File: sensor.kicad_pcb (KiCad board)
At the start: 2 copper layers, 62 x 65 mm, 94 parts, among them CON1 Micro USB, CON2 PROG, CON3 Jack-DC, CON4 HTU21D, CON5 Conn_01x08, Q1 BSS214N, Q2 BSS214N, Q3 BSS214N, Q4 BSP716N, Q5 BSP716N, Q6 BSP716N, SW1 RESET, SW2 CFG, U1 LM7805, U2 TLV1117LV33DCY, U3 ESP-12F, U4 HTU21D, U5 PMS7003

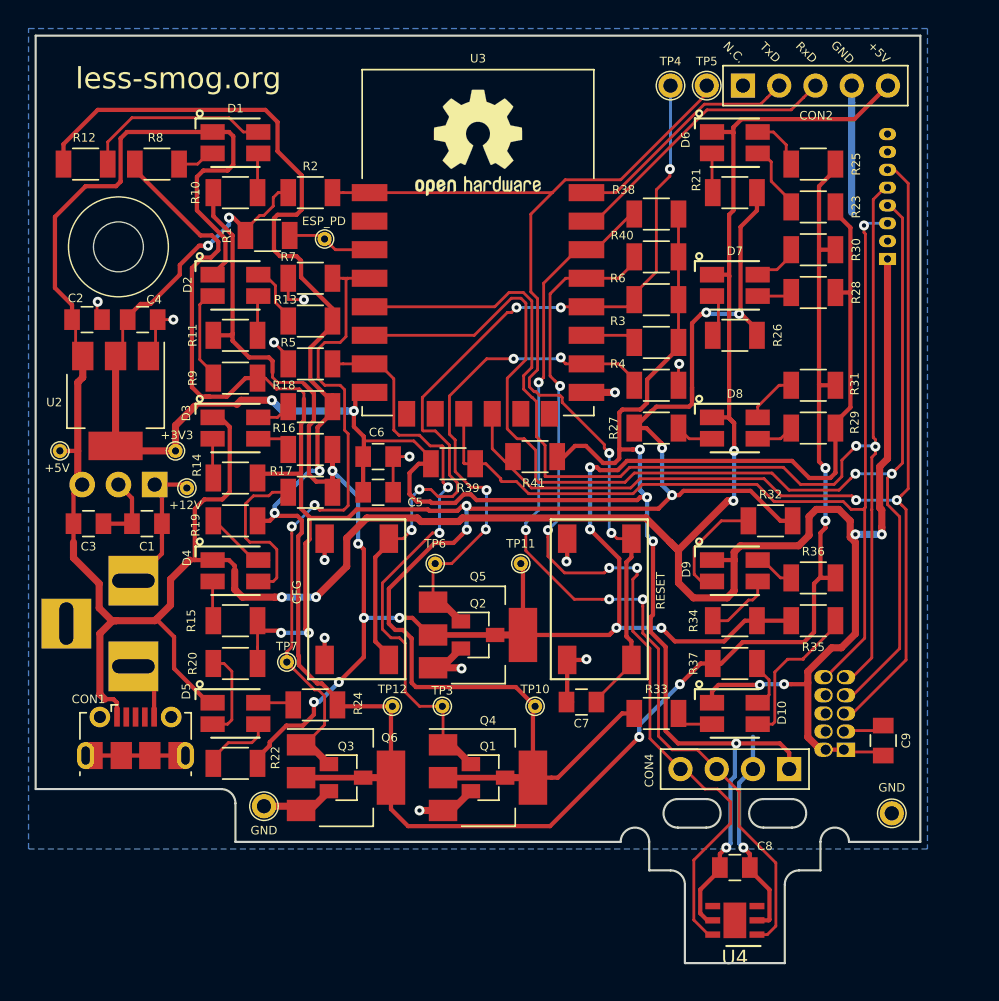
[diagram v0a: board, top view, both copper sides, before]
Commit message: Crudely routed board. Changed some footprints to easier to solder.
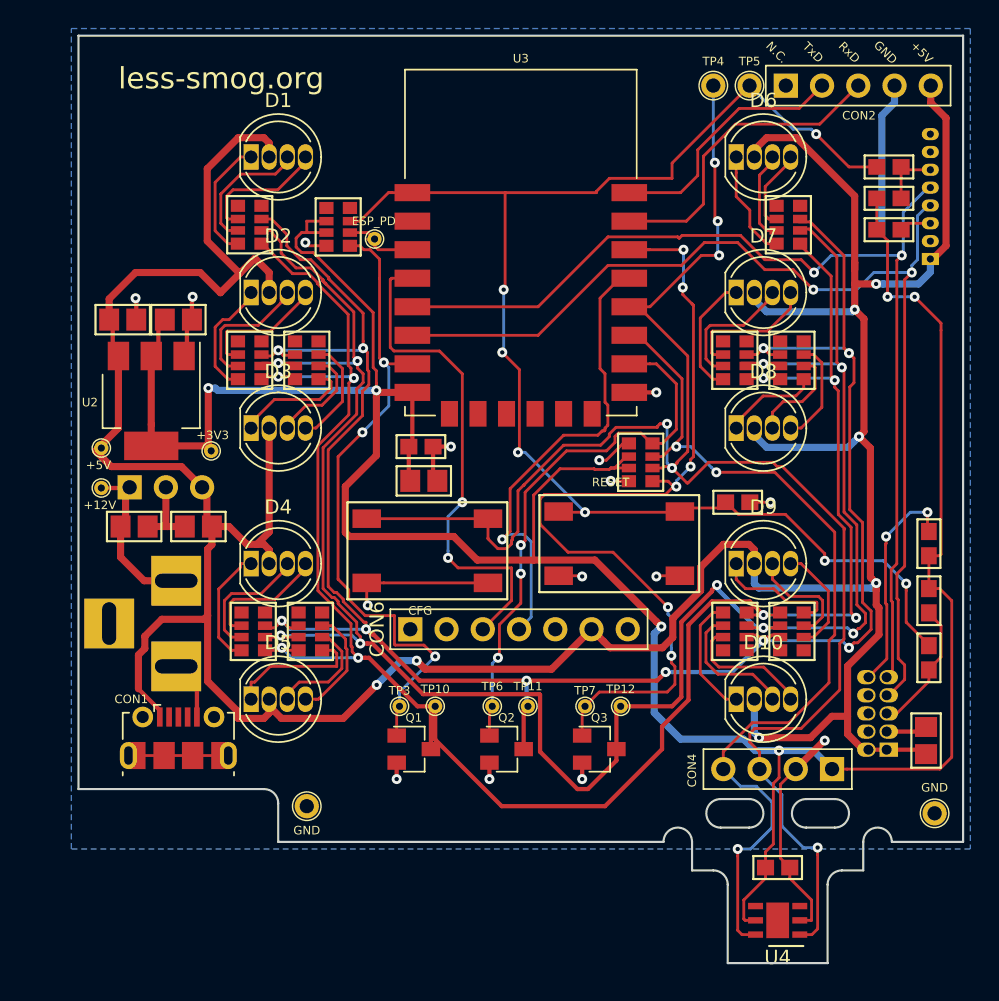
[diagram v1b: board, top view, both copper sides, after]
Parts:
- removed Q4, Q5, Q6: BSP716N, TO_SOT_Packages_SMD:SOT-223-3Lead_TabPin2
- removed R1, R2, R3, R38, R4, R40, R5, R6, R7: 10k, less-smog:R_1206
- removed R10, R13, R16, R17, R18, R19, R22, R23, R24, R25, R28, R29, R30, R31, R34, R35, R36, R37: 130, less-smog:R_1206
- removed R15, R20, R21, R26, R27, R32, R33, R8: 180, less-smog:R_1206
- removed REF***: OSHW-Logo2_9.8x8mm_SilkScreen, Symbols:OSHW-Logo2_9.8x8mm_SilkScreen
- removed REF***: KiCad-Logo2_6mm_SilkScreen, Symbols:KiCad-Logo2_6mm_SilkScreen
- added CON6: AUX, less-smog:E45-TTL-1W, F.Cu at (99.9, 83.1)
- added RN1: 150R, less-smog:4x0603_M, F.Cu at (81.0, 54.8)
- added RN10: 150R, less-smog:4x0603_M, F.Cu at (115.0, 83.2)
- added RN11: 10k, less-smog:4x0603_M, F.Cu at (108.4, 71.4)
- added RN12: 10k, less-smog:4x0603_M, F.Cu at (87.2, 54.9)
- added RN2: 150R, less-smog:4x0603_M, F.Cu at (81.0, 64.2)
- added RN3: 150R, less-smog:4x0603_M, F.Cu at (85.0, 64.2)
- added RN4: 150R, less-smog:4x0603_M, F.Cu at (81.2, 83.2)
- added RN5: 150R, less-smog:4x0603_M, F.Cu at (85.2, 83.2)
- added RN6: 150R, less-smog:4x0603_M, F.Cu at (118.8, 54.8)
- added RN7: 150R, less-smog:4x0603_M, F.Cu at (115.0, 64.2)
- added RN8: 150R, less-smog:4x0603_M, F.Cu at (119.0, 64.2)
- added RN9: 150R, less-smog:4x0603_M, F.Cu at (119.0, 83.2)
- C1: value 1uF/25V -> N.C.; footprint less-smog:C_0805 -> less-smog:0805_M
- C2, C4, C5, C9: footprint less-smog:C_0805 -> less-smog:0805_M
- C3: value 100nF -> N.C.; footprint less-smog:C_0805 -> less-smog:0805_M
- C6, C7, C8: footprint less-smog:C_0805 -> less-smog:0603_M
- CON3: value Jack-DC -> N.C.
- CON5: value Conn_01x08 -> PMS3003/5003
- D1, D10, D2, D3, D4, D5, D6, D7, D8, D9: value ASMB-MTB0-0A3A2 -> RGB 5mm; footprint less-smog:ASMB-MTB0-0A3A2 -> less-smog:LED_D5.0mm-4
- R11, R12: value 130 -> N.C.; footprint less-smog:R_1206 -> less-smog:0603_R_M
- R14, R9: value 180 -> N.C.; footprint less-smog:R_1206 -> less-smog:0603_R_M
- R39, R41: footprint less-smog:R_1206 -> less-smog:0603_R_M
- U1: value LM7805 -> N.C.; footprint TO_SOT_Packages_THT:TO-220_Horizontal -> less-smog:5V_DC_DC
- moved R12 56.4 mm to (125.8, 52.9)
- moved R9 52.4 mm to (128.6, 85.1), turned to 90 degrees
- moved R14 50.7 mm to (125.8, 50.7), turned to 180 degrees
- moved R11 46.4 mm to (125.8, 55.1)
- moved R39 33.8 mm to (128.6, 77.1), turned to 90 degrees
- moved R41 29.4 mm to (128.6, 81.1), turned to 270 degrees
- moved TP7 21.1 mm to (104.5, 88.5)
- moved Q3 17.9 mm to (105.5, 91.5)
- moved C7 17.8 mm to (115.2, 74.2), turned to 0 degrees
- moved TP12 16.0 mm to (107.0, 88.5)
- moved TP6 10.8 mm to (98.0, 88.5)
- moved TP11 10.0 mm to (100.5, 88.5)
- moved Q2 8.25 mm to (99.0, 91.5)
- moved C3 7.70 mm to (77.4, 75.9), turned to 180 degrees
- moved TP10 7.00 mm to (94.0, 88.5)
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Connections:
- CON4 pad 3: HTU_SDA -> HTU_SDA/CFG_BTN
- CON5 pad 3: PMS_SET -> Net-(CON5-Pad3)
- CON5 pad 6: PMS_RESET -> Net-(CON5-Pad6)
- D1 pad 1: +5V -> Net-(D1-Pad1)
- D1 pad 2: Net-(D1-Pad2) -> +5V
- D10 pad 1: +5V -> Net-(D10-Pad1)
- D10 pad 2: Net-(D10-Pad2) -> +5V
- D2 pad 1: +5V -> Net-(D2-Pad1)
- D2 pad 2: Net-(D2-Pad2) -> +5V
- D3 pad 1: +5V -> Net-(D3-Pad1)
- D3 pad 2: Net-(D3-Pad2) -> +5V
- D4 pad 1: +5V -> Net-(D4-Pad1)
- D4 pad 2: Net-(D4-Pad2) -> +5V
- D5 pad 1: +5V -> Net-(D5-Pad1)
- D5 pad 2: Net-(D5-Pad2) -> +5V
- D6 pad 1: +5V -> Net-(D6-Pad1)
- D6 pad 2: Net-(D6-Pad2) -> +5V
- D7 pad 1: +5V -> Net-(D7-Pad1)
- D7 pad 2: Net-(D7-Pad2) -> +5V
- D8 pad 1: +5V -> Net-(D8-Pad1)
- D8 pad 2: Net-(D8-Pad2) -> +5V
- D9 pad 1: +5V -> Net-(D9-Pad1)
- D9 pad 2: Net-(D9-Pad2) -> +5V
- R11 pad 1: Net-(D2-Pad3) -> Net-(CON5-Pad3)
- R11 pad 2: /LED_G -> +3V3
- R12 pad 1: Net-(D1-Pad2) -> Net-(CON5-Pad6)
- R12 pad 2: /LED_B -> +3V3
- R14 pad 1: Net-(D3-Pad4) -> Net-(CON5-Pad6)
- R14 pad 2: /LED_R -> RESET
- R39 pad 2: PMS_SET -> Net-(R39-Pad2)
- R41 pad 2: PMS_RESET -> Net-(R41-Pad2)
- R9 pad 1: Net-(D2-Pad4) -> Net-(R41-Pad2)
- R9 pad 2: /LED_R -> RESET
- SW2 pad 1: CFG_BTN -> HTU_SDA/CFG_BTN
- TP4 pad 1: CFG_BTN -> HTU_SDA/CFG_BTN
- U3 pad 11: PMS_SET -> (no net)
- U3 pad 12: PMS_RESET -> (no net)
- U3 pad 17: /BOOT1 -> HTU_SCL
- U3 pad 18: CFG_BTN -> HTU_SDA/CFG_BTN
- U3 pad 19: HTU_SCL -> GPIO4
- U3 pad 20: HTU_SDA -> LED_B_CTRL
- U3 pad 4: LED_B_CTRL -> GPIO16
- U4 pad 1: HTU_SDA -> HTU_SDA/CFG_BTN
- U5 pad 10: PMS_SET -> Net-(R39-Pad2)
- U5 pad 5: PMS_RESET -> Net-(R41-Pad2)
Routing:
- net HTU_SDA/CFG_BTN: track 0.00 -> 118.6 mm, vias 0 -> 6
- net PMS_RESET: track 74.8 -> 0.00 mm, vias 2 -> 0
- net PMS_SET: track 68.9 -> 0.00 mm, vias 1 -> 0
- net HTU_SDA: track 66.6 -> 0.00 mm, vias 4 -> 0
- net CFG_BTN: track 59.1 -> 0.00 mm, vias 5 -> 0
- net +3V3: track 156.1 -> 193.0 mm, vias 9 -> 6
- net GPIO16: track 0.00 -> 35.3 mm, vias 0 -> 2
- net GPIO4: track 0.00 -> 33.2 mm, vias 0 -> 1
- net /LED_R: track 173.3 -> 142.2 mm
- net RESET: track 72.2 -> 101.5 mm, vias 2 -> 7
- net LED_B_CTRL: track 46.4 -> 62.2 mm, vias 2 -> 6
- net Net-(R39-Pad2): track 0.00 -> 15.5 mm, vias 0 -> 2
- net PMS_RXD: track 90.1 -> 75.8 mm
- net /LED_B: track 162.6 -> 148.3 mm, vias 6 -> 9
- net Net-(D1-Pad2): track 14.1 -> 0.00 mm
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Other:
- net class Default: clearance 0.2 -> 0.16
- net class Power: clearance 0.2 -> 0.16
- rule trace_clearance: 0.2 -> 0.16
- board text removed: "PMS3003/5003"
- board text removed: "PMS7003"

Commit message: Routing optimization
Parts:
- moved TP1 0.35 mm to (89.8, 55.4)
- moved RN5 0.25 mm to (85.2, 83.5)
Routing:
- net /LED_G: track 140.5 -> 154.3 mm
- net /LED_B: track 148.3 -> 155.3 mm
- net LED_B_CTRL: track 62.2 -> 68.4 mm, vias 6 -> 4
- net +3V3: track 193.0 -> 187.5 mm, vias 6 -> 4
- net /LED_R: track 142.2 -> 145.7 mm
- net Net-(D8-Pad1): track 6.73 -> 9.06 mm
- net RESET: track 101.5 -> 103.7 mm
- net Net-(R39-Pad2): track 15.5 -> 17.6 mm
- net HTU_SDA/CFG_BTN: track 118.6 -> 120.7 mm
- net LED_G_CTRL: track 38.4 -> 40.1 mm
- net GND: track 80.0 -> 78.4 mm
- net +5V: track 252.7 -> 251.4 mm, vias 7 -> 8
- net PMS_RXD: track 75.8 -> 74.6 mm
- net HTU_SCL: track 63.1 -> 64.3 mm
- net ESP_RXD: track 21.9 -> 20.8 mm
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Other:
- board text added: "Licensed under CERN Open Hardware License 1.2 Revision 2"
- board text removed: "Licensed under CERN Open Hardware License 1.2 Revision 1"

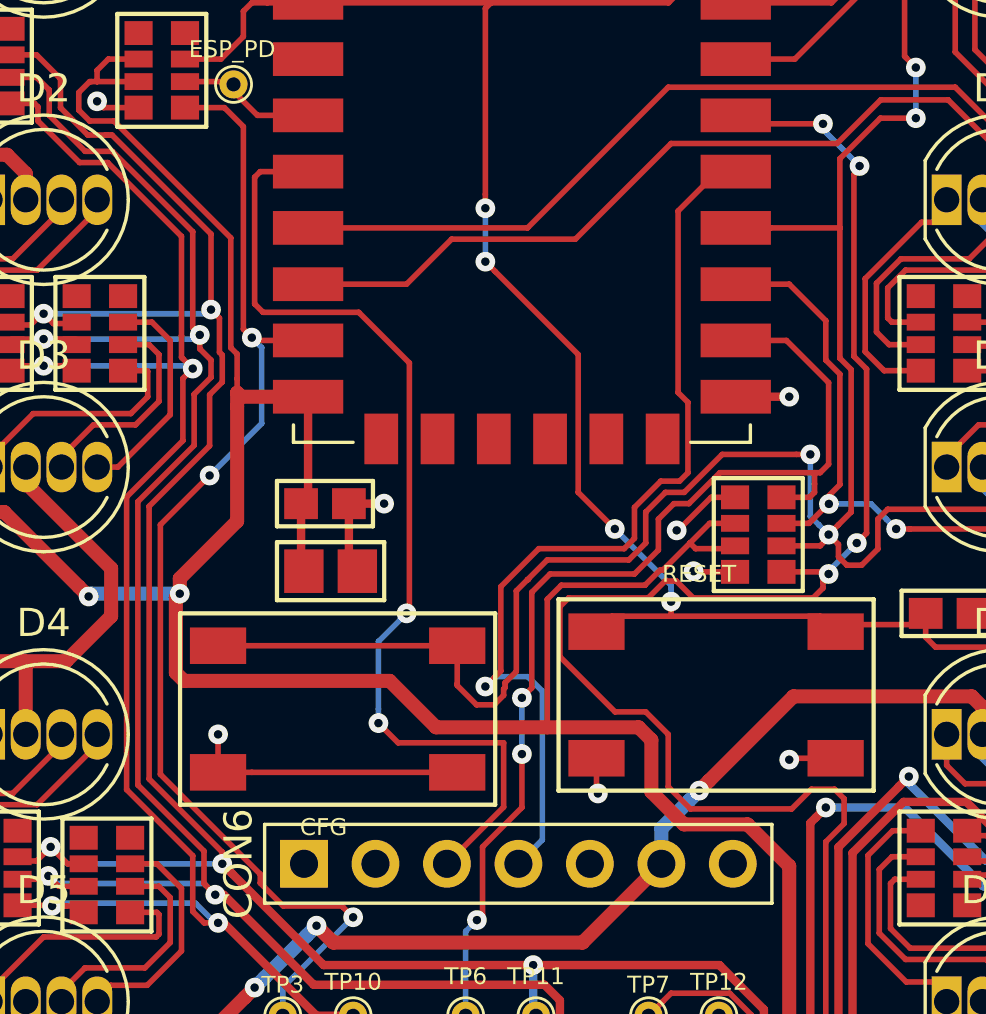
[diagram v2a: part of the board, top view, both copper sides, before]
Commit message: Button position correction
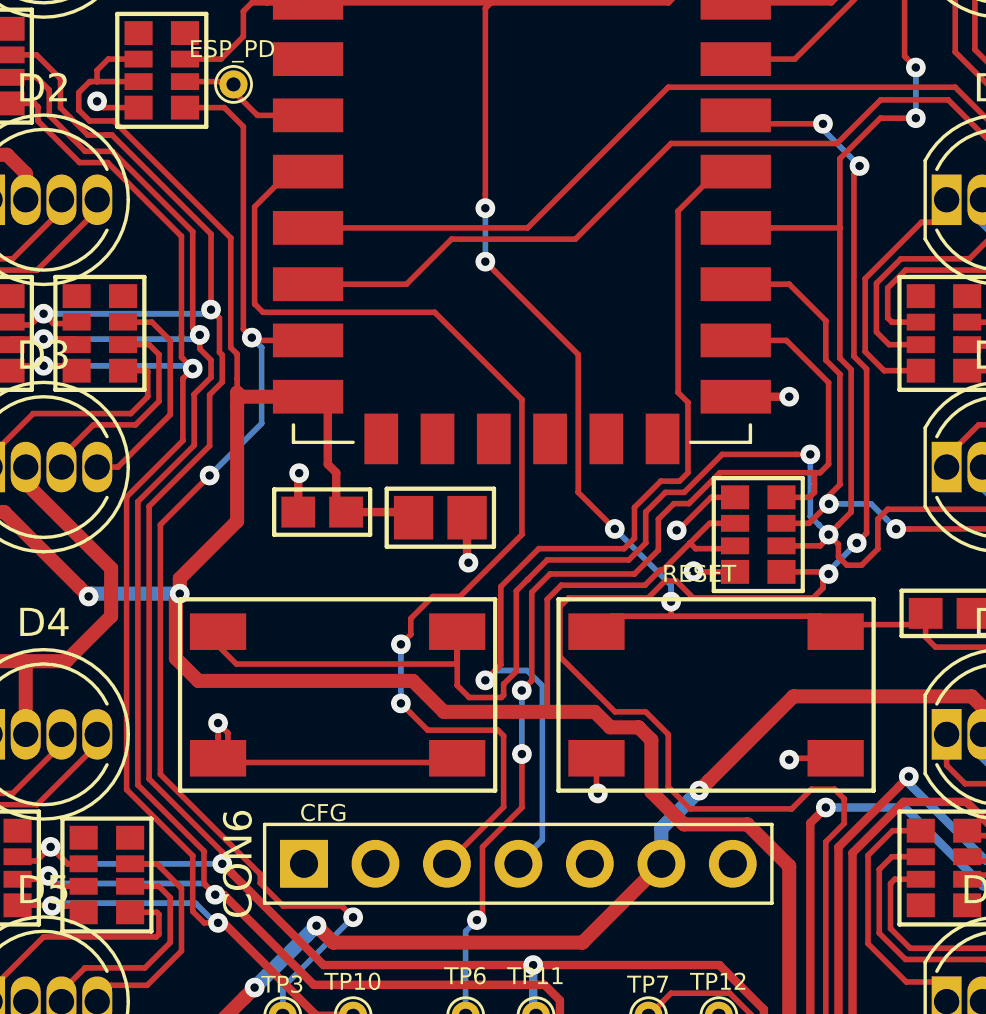
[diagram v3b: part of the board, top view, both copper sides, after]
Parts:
- moved C5 4.34 mm to (97.1, 70.8)
- moved SW2 0.50 mm to (93.5, 77.1)
- moved C6 0.32 mm to (92.9, 70.6), turned to 180 degrees
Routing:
- net GPIO16: track 36.0 -> 39.4 mm
- net HTU_SDA/CFG_BTN: track 120.7 -> 122.4 mm
- net GND: track 78.4 -> 79.4 mm, vias 15 -> 16

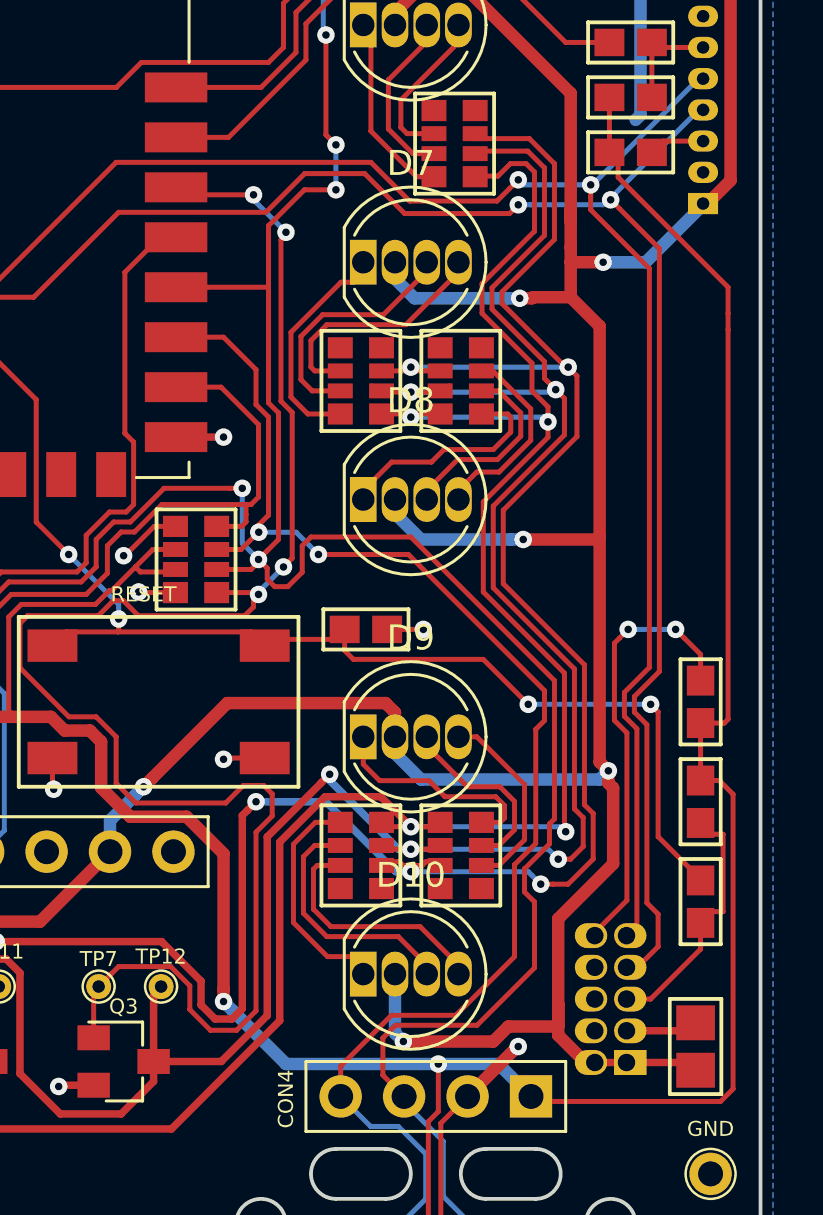
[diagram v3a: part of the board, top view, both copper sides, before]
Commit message: Add connector for SDS011 Close #10
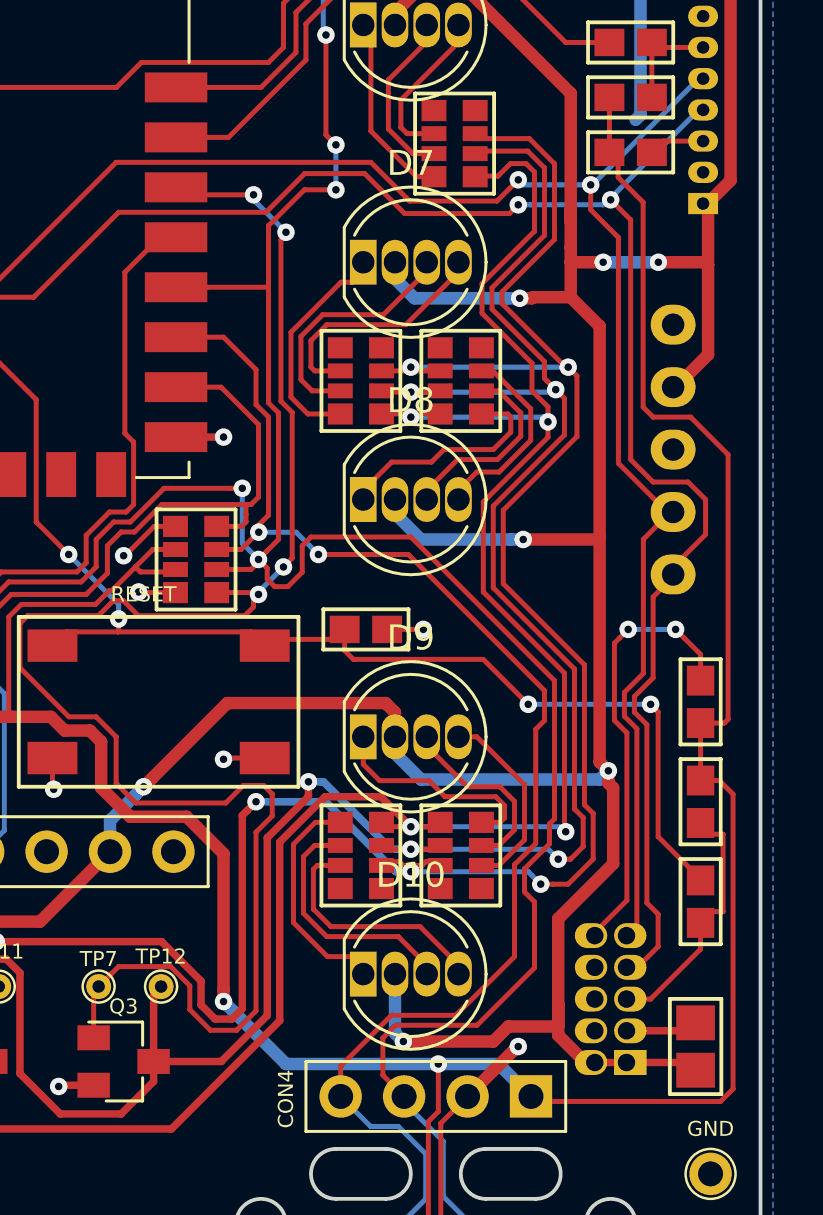
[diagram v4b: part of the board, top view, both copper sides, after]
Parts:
- added CON7: Conn_01x05, less-smog:B5B-XH-A(LF)(SN), B.Cu at (127.5, 67.0)
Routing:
- net +5V: track 251.4 -> 258.9 mm, vias 8 -> 9
- net PMS_RXD: track 74.6 -> 76.9 mm
- net PMS_TXD: track 73.0 -> 74.0 mm
- net +3V3: track 187.7 -> 188.6 mm

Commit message: Update silkscreen
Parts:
- CON7: value Conn_01x05 -> SDS011
